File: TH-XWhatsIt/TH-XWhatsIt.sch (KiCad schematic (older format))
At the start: 26 parts, among them J1 MODEL F, J2 EXPANSION, J3 EXPANSION HEADER, U1 MCP4921-EP, U2 LM339, U3 74HCT595, U4 74HCT595, U5 ProMicro, U6 LM339, U7 74HCT595

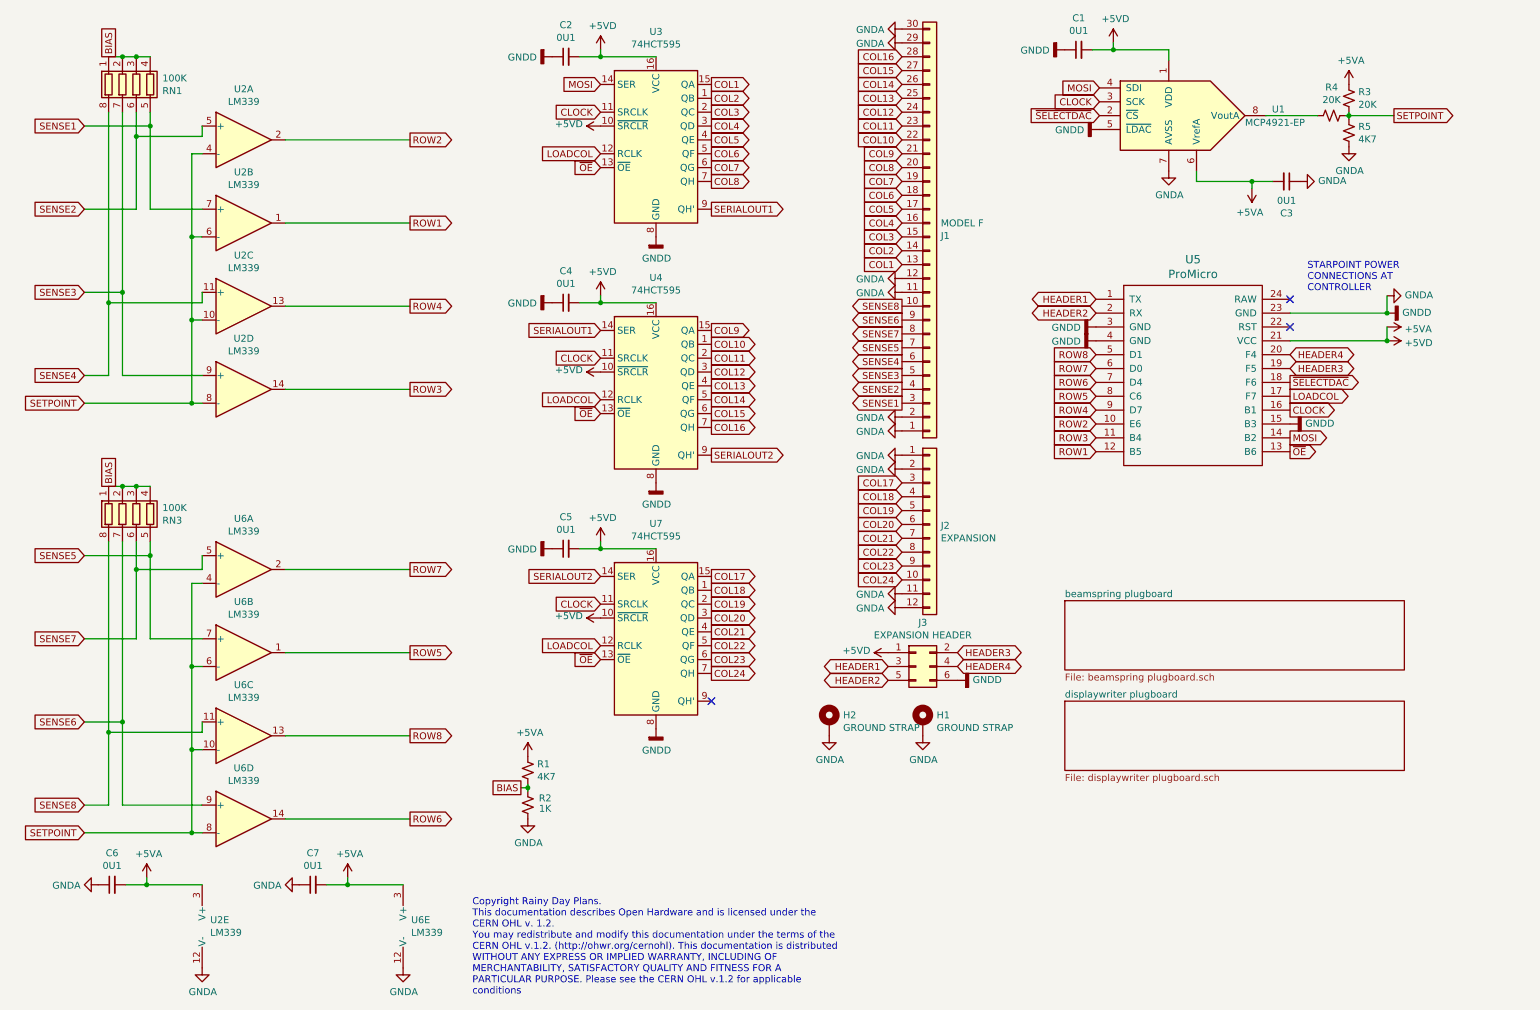
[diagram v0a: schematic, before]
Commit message: Schematics: shift register OE pins connected to GND, and unused ProMicro pin connected to gnd
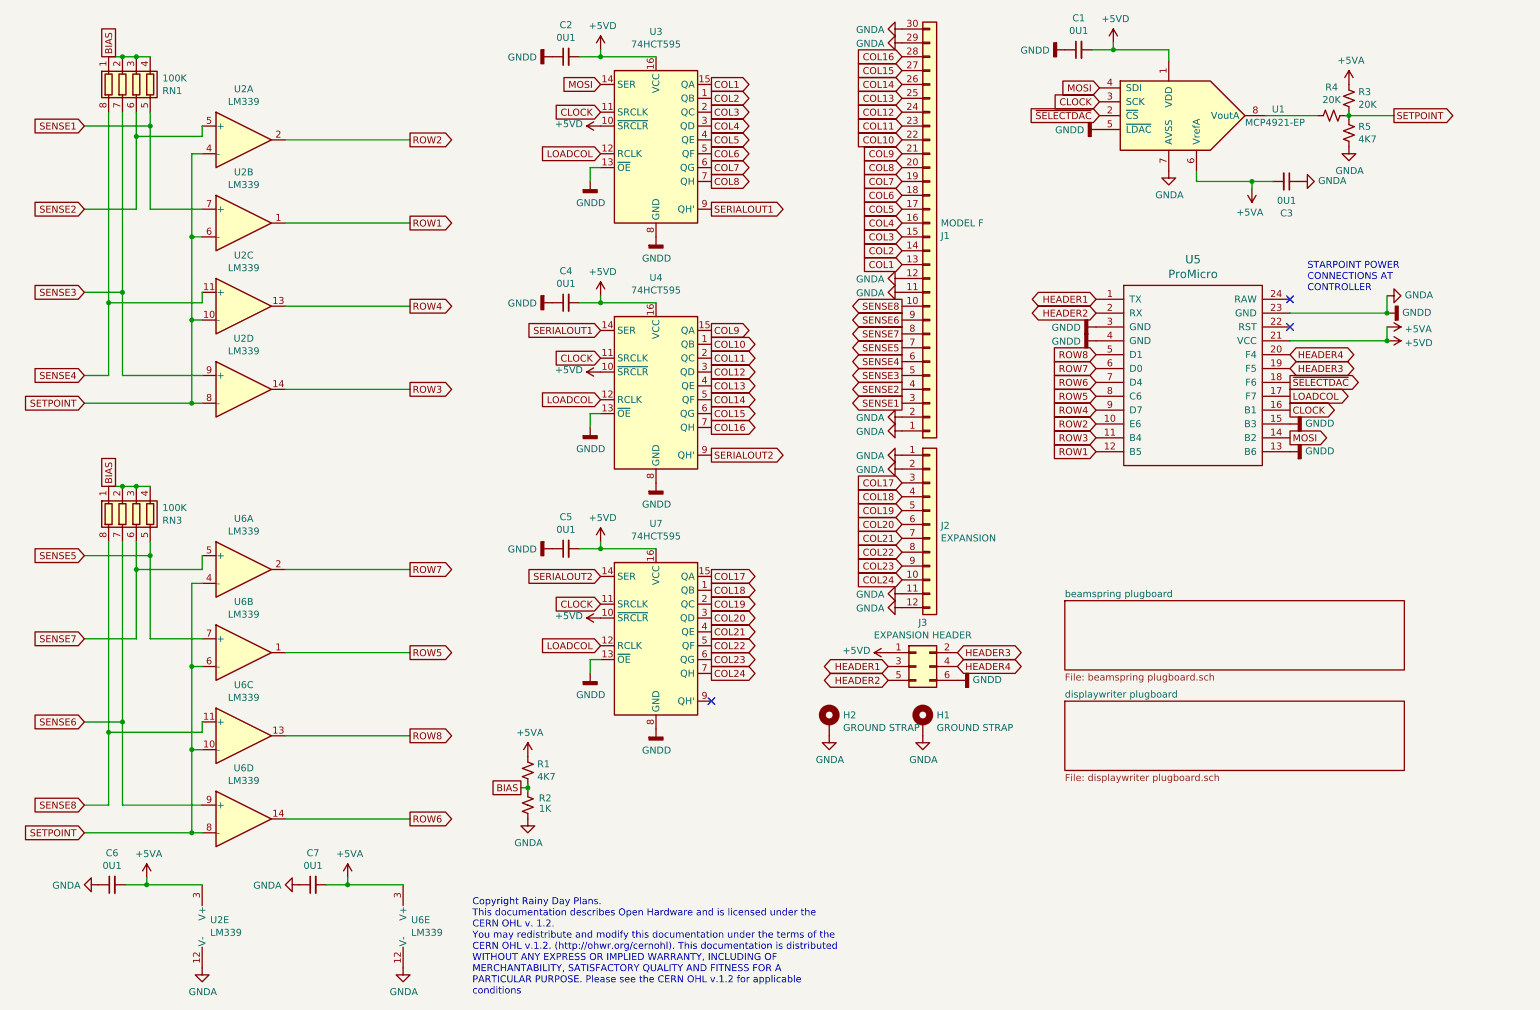
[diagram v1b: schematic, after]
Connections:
- net ~OE is gone; now on net GNDA: U3.13 (~OE), U4.13 (~OE), U5.13 (B6), U7.13 (~OE)
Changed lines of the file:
@@
 Text GLabel 4875 1375 0    50   Input ~ 0
 CLOCK
-Text GLabel 4875 1775 0    50   Input ~ 0
-~OE
 Wire Wire Line
 	2000 4775 1925 4775
@@
 Wire Wire Line
 	4875 2700 4875 2750
-Text GLabel 4875 3550 0    50   Input ~ 0
-~OE
 $Comp
 L 74xx:74HCT595 U7
@@
 Wire Wire Line
 	4875 4475 4875 4525
-Text GLabel 4875 5325 0    50   Input ~ 0
-~OE
 Text GLabel 5675 2075 2    50   Output ~ 0
 SERIALOUT1
@@
 Text GLabel 9850 3425 2    50   Output ~ 0
 LOADCOL
-Text GLabel 9850 3825 2    50   Output ~ 0
-~OE
 Text GLabel 7050 1675 0    50   Input ~ 0
 COL9
@@
 	1    0    0    -1
 $EndComp
+$Comp
+L power:GNDD #PWR?
+U 1 1 5F38CBA0
+P 4800 1875
+F 0 "#PWR?" H 4800 1625 50  0001 C CNN
+F 1 "GNDD" H 4804 1720 50  0000 C CNN
+F 2 "" H 4800 1875 50  0001 C CNN
+F 3 "" H 4800 1875 50  0001 C CNN
+	1    4800 1875
+	1    0    0    -1
+$EndComp
+$Comp
+L power:GNDD #PWR?
+U 1 1 5F38E20D
+P 4800 3650
+F 0 "#PWR?" H 4800 3400 50  0001 C CNN
+F 1 "GNDD" H 4804 3495 50  0000 C CNN
+F 2 "" H 4800 3650 50  0001 C CNN
+F 3 "" H 4800 3650 50  0001 C CNN
+	1    4800 3650
+	1    0    0    -1
+$EndComp
+Wire Wire Line
+	4800 1875 4800 1775
+Wire Wire Line
+	4800 1775 4875 1775
+Wire Wire Line
+	4800 3650 4800 3550
+Wire Wire Line
+	4800 3550 4875 3550
+$Comp
+L power:GNDD #PWR?
+U 1 1 5F39B529
+P 4800 5425
+F 0 "#PWR?" H 4800 5175 50  0001 C CNN
+F 1 "GNDD" H 4804 5270 50  0000 C CNN
+F 2 "" H 4800 5425 50  0001 C CNN
+F 3 "" H 4800 5425 50  0001 C CNN
+	1    4800 5425
+	1    0    0    -1
+$EndComp
+Wire Wire Line
+	4800 5425 4800 5325
+Wire Wire Line
+	4800 5325 4875 5325
+$Comp
+L power:GNDD #PWR?
+U 1 1 5F3A2D72
+P 9850 3825
+F 0 "#PWR?" H 9850 3575 50  0001 C CNN
+F 1 "GNDD" V 9854 3715 50  0000 R CNN
+F 2 "" H 9850 3825 50  0001 C CNN
+F 3 "" H 9850 3825 50  0001 C CNN
+	1    9850 3825
+	0    -1   -1   0
+$EndComp
 $EndSCHEMATC

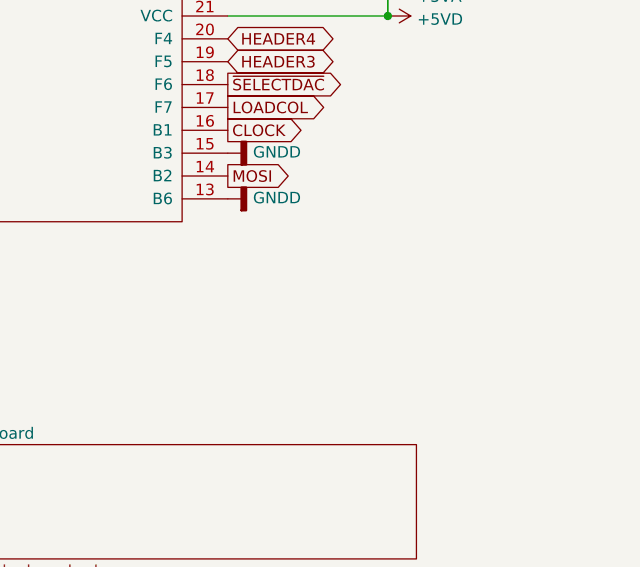
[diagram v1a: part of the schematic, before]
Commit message: Schematic: added note about the purpose of the grounded promicro pins
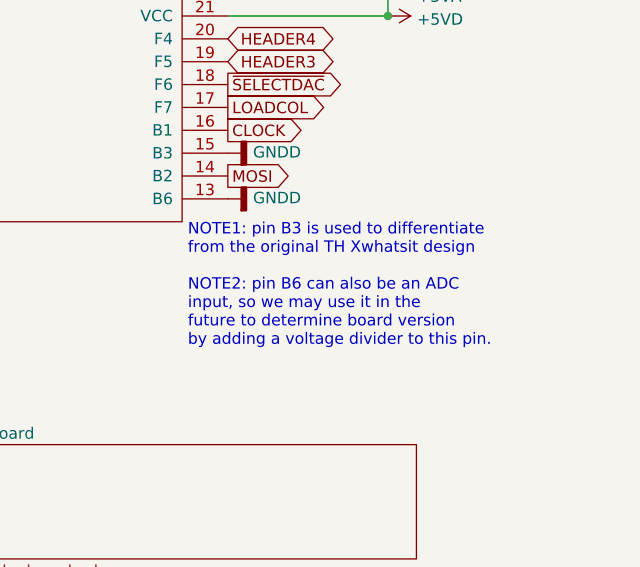
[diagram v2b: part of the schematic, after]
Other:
- note added: "NOTE1: pin B3 is used to differentiate\nfrom the original TH Xwhatsit design\n\nNOTE2: pin B6 can also be an ADC\ninput, so we may use it in the\nfuture to determine board version\nby adding a voltage divider to this pin."
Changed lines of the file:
@@
 	0    -1   -1   0
 $EndComp
+Text Notes 9675 4475 0    50   ~ 0
+NOTE1: pin B3 is used to differentiate\nfrom the original TH Xwhatsit design\n\nNOTE2: pin B6 can also be an ADC\ninput, so we may use it in the\nfuture to determine board version\nby adding a voltage divider to this pin.
 $EndSCHEMATC

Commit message: pcb: made solenoid header footprint vertical, removed right side of controller PCB
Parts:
- J3: footprint Connector_PinHeader_2.54mm:PinHeader_2x03_P2.54mm_Horizontal -> Connector_PinHeader_2.54mm:PinHeader_2x03_P2.54mm_Vertical
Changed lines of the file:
@@
 F 0 "J3" H 7200 5692 50  0000 C CNN
 F 1 "EXPANSION HEADER" H 7200 5601 50  0000 C CNN
-F 2 "Connector_PinHeader_2.54mm:PinHeader_2x03_P2.54mm_Horizontal" H 7150 5375 50  0001 C CNN
+F 2 "Connector_PinHeader_2.54mm:PinHeader_2x03_P2.54mm_Vertical" H 7150 5375 50  0001 C CNN
 F 3 "~" H 7150 5375 50  0001 C CNN
 	1    7150 5375

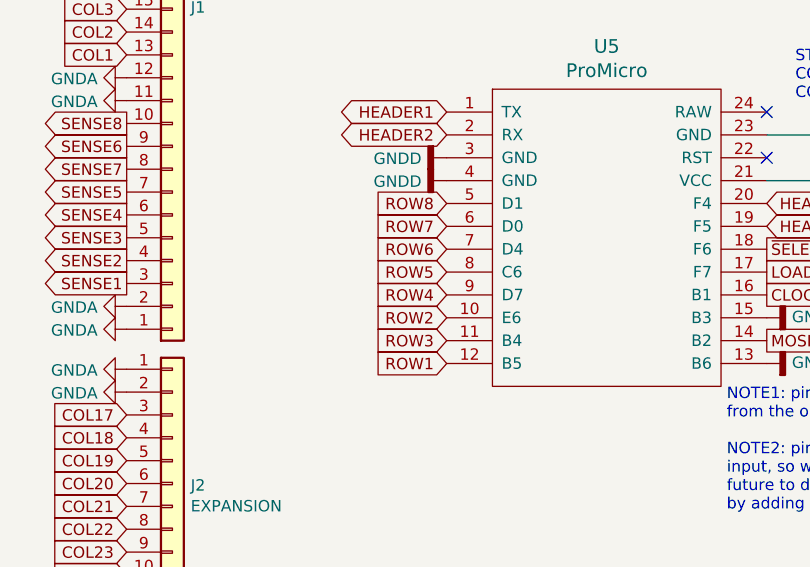
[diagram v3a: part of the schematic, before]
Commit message: Reordered row to promicro pin connections to make sure that beamsprings only use two different ports
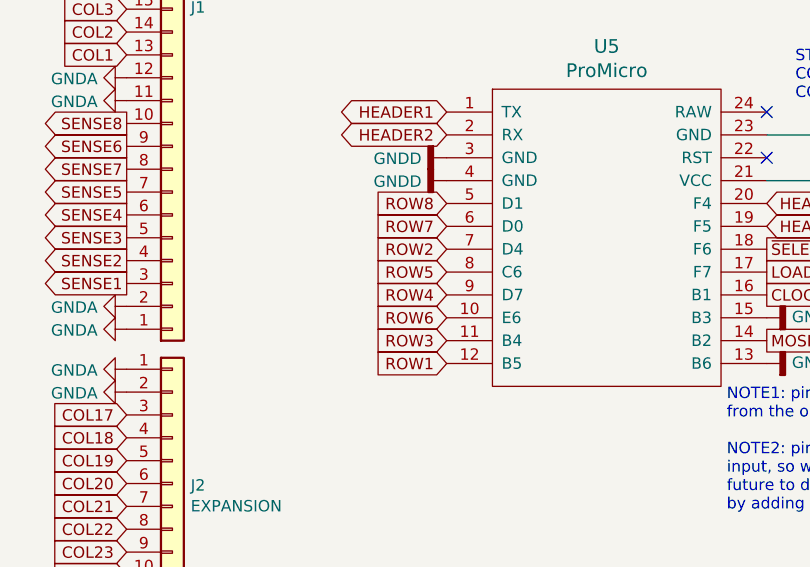
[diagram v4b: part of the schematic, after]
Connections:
- net ROW2: now also U5.7 (D4); no longer U5.10 (E6)
- net ROW6: now also U5.10 (E6); no longer U5.7 (D4)
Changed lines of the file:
@@
 Text GLabel 8450 3825 0    50   Input ~ 0
 ROW1
-Text GLabel 8450 3625 0    50   Input ~ 0
+Text GLabel 8450 3325 0    50   Input ~ 0
 ROW2
 Text GLabel 8450 3725 0    50   Input ~ 0
@@
 Text GLabel 8450 3425 0    50   Input ~ 0
 ROW5
-Text GLabel 8450 3325 0    50   Input ~ 0
+Text GLabel 8450 3625 0    50   Input ~ 0
 ROW6
 Text GLabel 8450 3225 0    50   Input ~ 0

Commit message: changed resistor network footprint sizes to what's available from jlcpcb
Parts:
- RN1, RN3: footprint Resistor_SMD:R_Array_Convex_4x1206 -> Resistor_SMD:R_Array_Convex_4x0603
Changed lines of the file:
@@
 F 0 "RN3" H 1713 4321 50  0000 L CNN
 F 1 "100K" H 1713 4230 50  0000 L CNN
-F 2 "Resistor_SMD:R_Array_Convex_4x1206" V 1800 4275 50  0001 C CNN
+F 2 "Resistor_SMD:R_Array_Convex_4x0603" V 1800 4275 50  0001 C CNN
 F 3 "~" H 1525 4275 50  0001 C CNN
 	1    1525 4275
@@
 F 0 "RN1" H 1713 1221 50  0000 L CNN
 F 1 "100K" H 1713 1130 50  0000 L CNN
-F 2 "Resistor_SMD:R_Array_Convex_4x1206" V 1800 1175 50  0001 C CNN
+F 2 "Resistor_SMD:R_Array_Convex_4x0603" V 1800 1175 50  0001 C CNN
 F 3 "~" H 1525 1175 50  0001 C CNN
 	1    1525 1175
@@
 $EndComp
 $Comp
-L power:GNDD #PWR?
+L power:GNDD #PWR0104
 U 1 1 5F38CBA0
 P 4800 1875
-F 0 "#PWR?" H 4800 1625 50  0001 C CNN
+F 0 "#PWR0104" H 4800 1625 50  0001 C CNN
 F 1 "GNDD" H 4804 1720 50  0000 C CNN
 F 2 "" H 4800 1875 50  0001 C CNN
@@
 $EndComp
 $Comp
-L power:GNDD #PWR?
+L power:GNDD #PWR0105
 U 1 1 5F38E20D
 P 4800 3650
-F 0 "#PWR?" H 4800 3400 50  0001 C CNN
+F 0 "#PWR0105" H 4800 3400 50  0001 C CNN
 F 1 "GNDD" H 4804 3495 50  0000 C CNN
 F 2 "" H 4800 3650 50  0001 C CNN
@@
 	4800 3550 4875 3550
 $Comp
-L power:GNDD #PWR?
+L power:GNDD #PWR0106
 U 1 1 5F39B529
 P 4800 5425
-F 0 "#PWR?" H 4800 5175 50  0001 C CNN
+F 0 "#PWR0106" H 4800 5175 50  0001 C CNN
 F 1 "GNDD" H 4804 5270 50  0000 C CNN
 F 2 "" H 4800 5425 50  0001 C CNN
@@
 	4800 5325 4875 5325
 $Comp
-L power:GNDD #PWR?
+L power:GNDD #PWR0107
 U 1 1 5F3A2D72
 P 9850 3825
-F 0 "#PWR?" H 9850 3575 50  0001 C CNN
+F 0 "#PWR0107" H 9850 3575 50  0001 C CNN
 F 1 "GNDD" V 9854 3715 50  0000 R CNN
 F 2 "" H 9850 3825 50  0001 C CNN

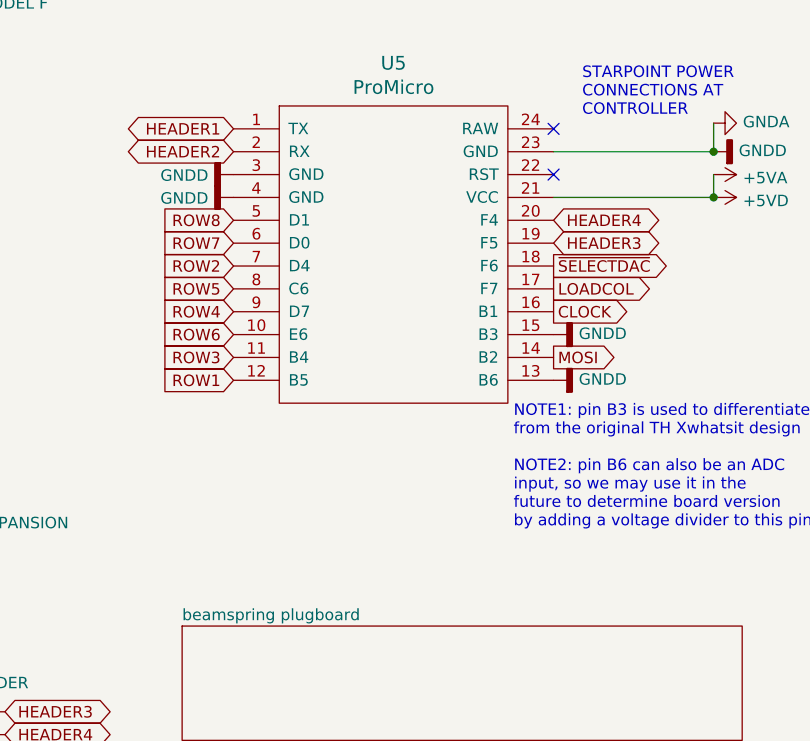
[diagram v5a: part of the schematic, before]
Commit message: Added pads for easily shorting reset with a screwdriver
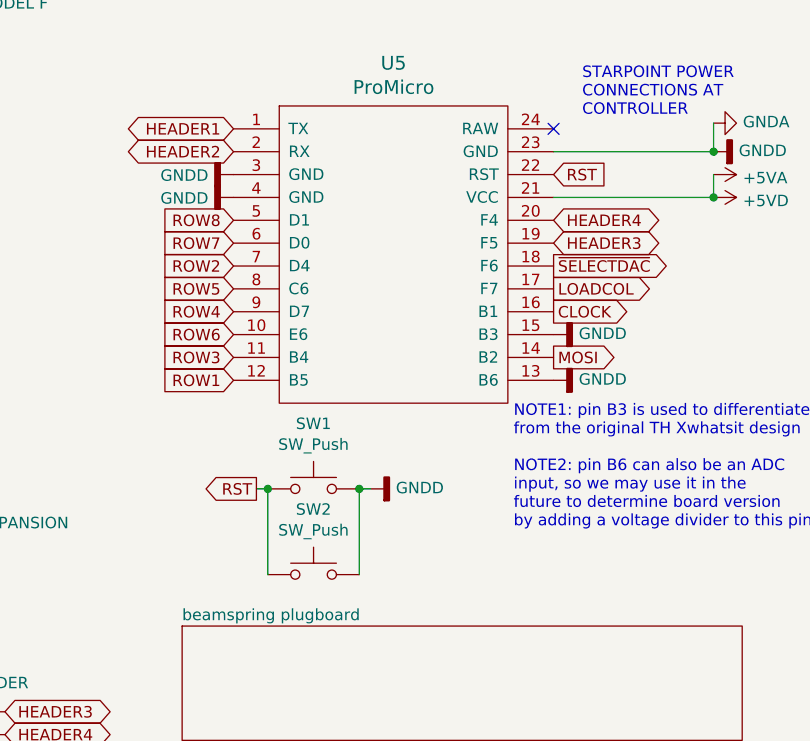
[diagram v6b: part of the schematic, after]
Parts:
- added SW1, SW2: SW_Push, TH-XWhatsIt:PadsToShort, symbol Switch:SW_Push
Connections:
- net GNDA: now also SW1.2, SW2.2
- net RST: now reaches U5.22 (RST)
- net RST: now also SW1.1, SW2.1
- no-connect marks 3 -> 2
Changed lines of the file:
@@
 CLOCK
 NoConn ~ 9850 2725
-NoConn ~ 9850 2925
 Text GLabel 8450 3825 0    50   Input ~ 0
 ROW1
@@
 Text Notes 9675 4475 0    50   ~ 0
 NOTE1: pin B3 is used to differentiate\nfrom the original TH Xwhatsit design\n\nNOTE2: pin B6 can also be an ADC\ninput, so we may use it in the\nfuture to determine board version\nby adding a voltage divider to this pin.
+$Comp
+L power:GNDD #PWR0108
+U 1 1 5F3F2027
+P 9050 4300
+F 0 "#PWR0108" H 9050 4050 50  0001 C CNN
+F 1 "GNDD" V 9054 4190 50  0000 R CNN
+F 2 "" H 9050 4300 50  0001 C CNN
+F 3 "" H 9050 4300 50  0001 C CNN
+	1    9050 4300
+	0    -1   -1   0
+$EndComp
+Text GLabel 8550 4300 0    50   Output ~ 0
+RST
+Text GLabel 9850 2925 2    50   Input ~ 0
+RST
+$Comp
+L Switch:SW_Push SW1
+U 1 1 5F4075C4
+P 8800 4300
+F 0 "SW1" H 8800 4585 50  0000 C CNN
+F 1 "SW_Push" H 8800 4494 50  0000 C CNN
+F 2 "TH-XWhatsIt:PadsToShort" H 8800 4500 50  0001 C CNN
+F 3 "" H 8800 4500 50  0001 C CNN
+	1    8800 4300
+	1    0    0    -1
+$EndComp
+$Comp
+L Switch:SW_Push SW2
+U 1 1 5F44B2D2
+P 8800 4675
+F 0 "SW2" H 8800 4960 50  0000 C CNN
+F 1 "SW_Push" H 8800 4869 50  0000 C CNN
+F 2 "TH-XWhatsIt:PadsToShort" H 8800 4875 50  0001 C CNN
+F 3 "" H 8800 4875 50  0001 C CNN
+	1    8800 4675
+	1    0    0    -1
+$EndComp
+Wire Wire Line
+	8600 4300 8600 4675
+Wire Wire Line
+	9000 4675 9000 4300
+Connection ~ 9000 4300
+Wire Wire Line
+	9000 4300 9050 4300
+Wire Wire Line
+	8600 4300 8550 4300
+Connection ~ 8600 4300
 $EndSCHEMATC
